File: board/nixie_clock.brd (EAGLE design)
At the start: 130 x 79 mm, 45 parts, among them Q1 BC546B, U1 AMS1117-5.0, U2 SN74141N

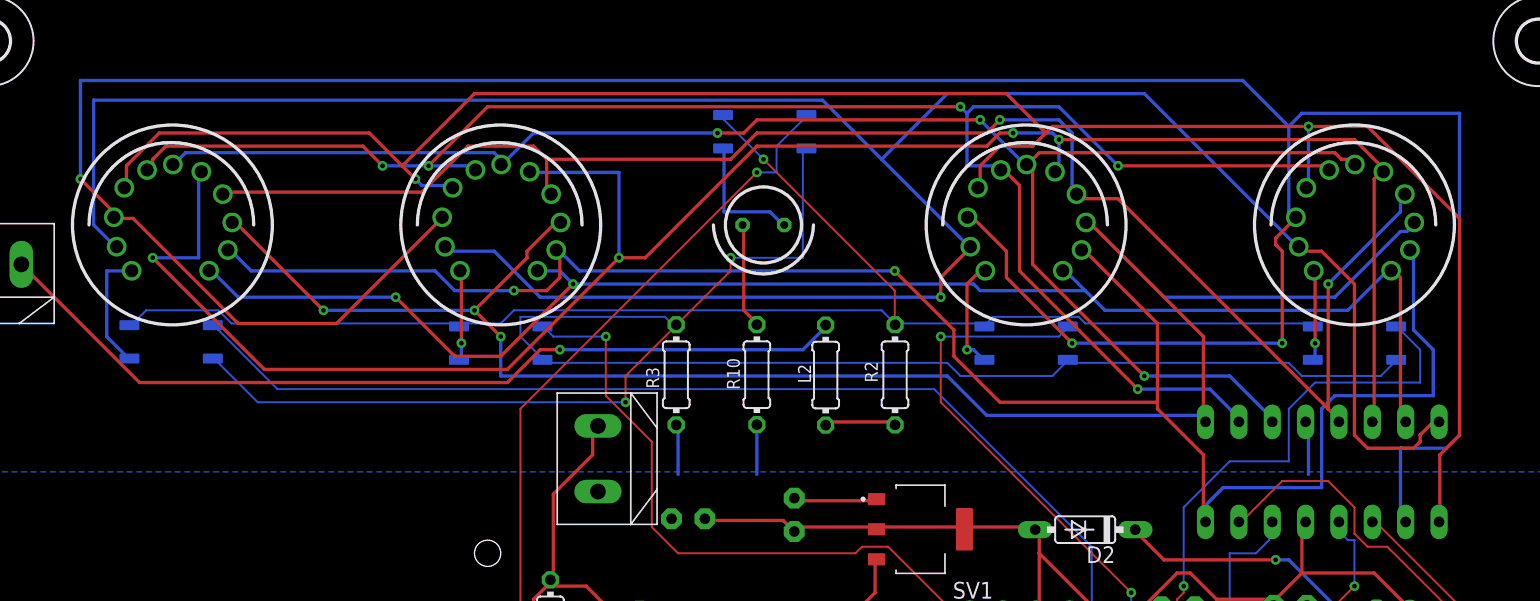
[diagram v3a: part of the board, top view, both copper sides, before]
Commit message: rounded off 90 degree wire turns
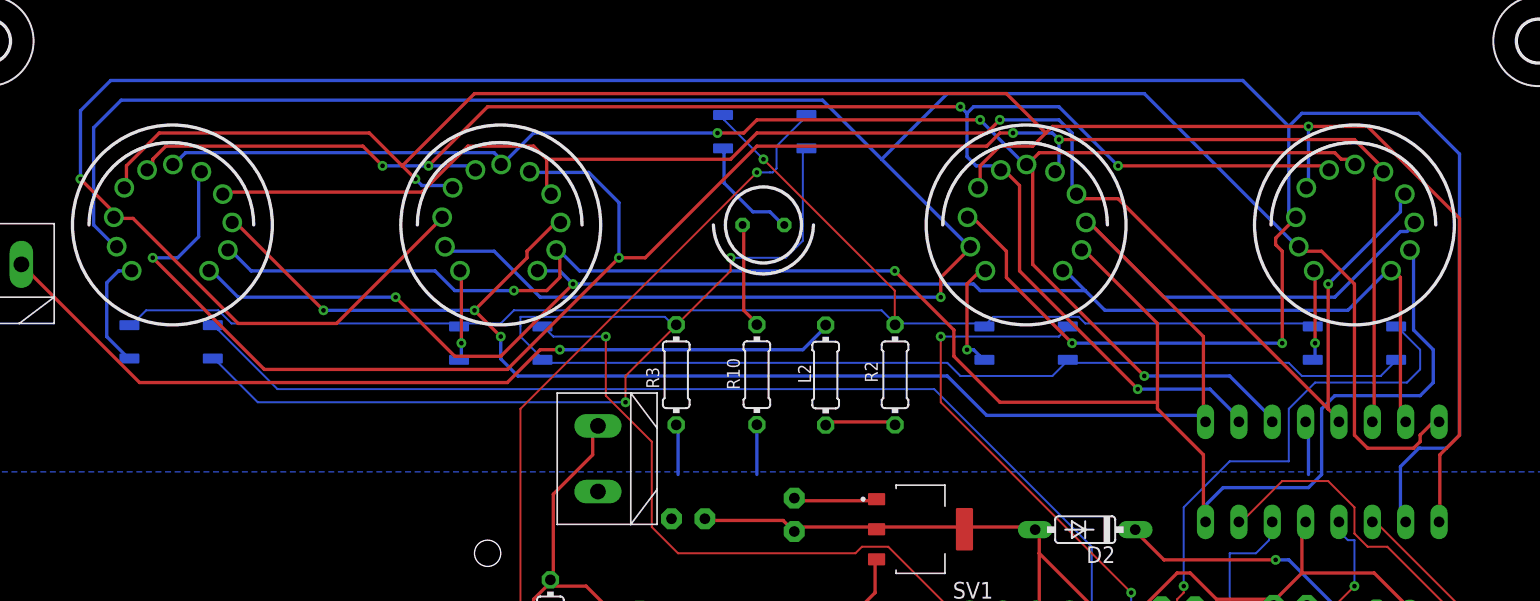
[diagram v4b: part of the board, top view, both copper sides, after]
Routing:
- net K9: track 232.2 -> 228.3 mm
- net K5: track 151.5 -> 149.2 mm
- net A_DOT: track 9.84 -> 8.55 mm
- net K0: track 191.0 -> 189.7 mm
- net K2: track 143.3 -> 142.2 mm
- net K3: track 141.0 -> 140.3 mm
- net N$16: track 144.1 -> 143.3 mm
- net N$3: track 61.8 -> 61.2 mm
- net A_10H: track 9.30 -> 8.77 mm

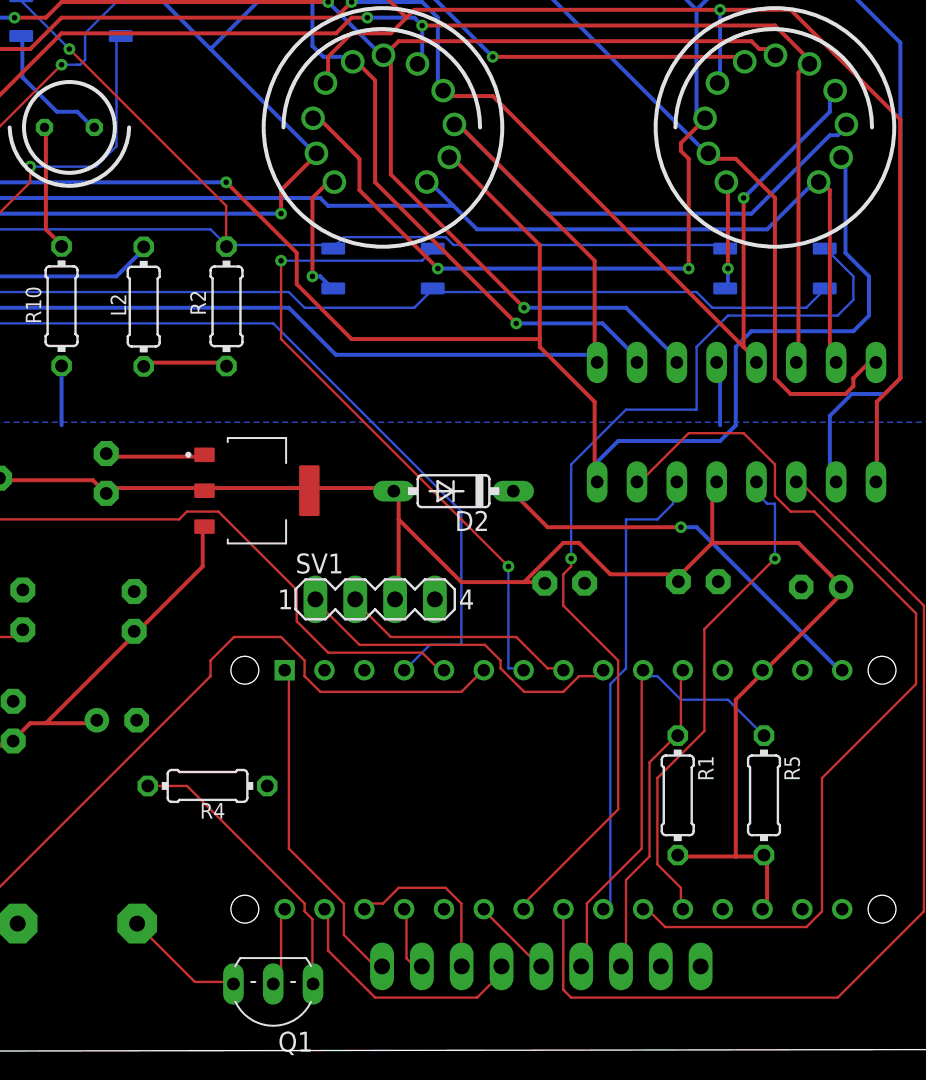
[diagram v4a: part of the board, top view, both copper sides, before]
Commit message: Connected 12V to buzzer.
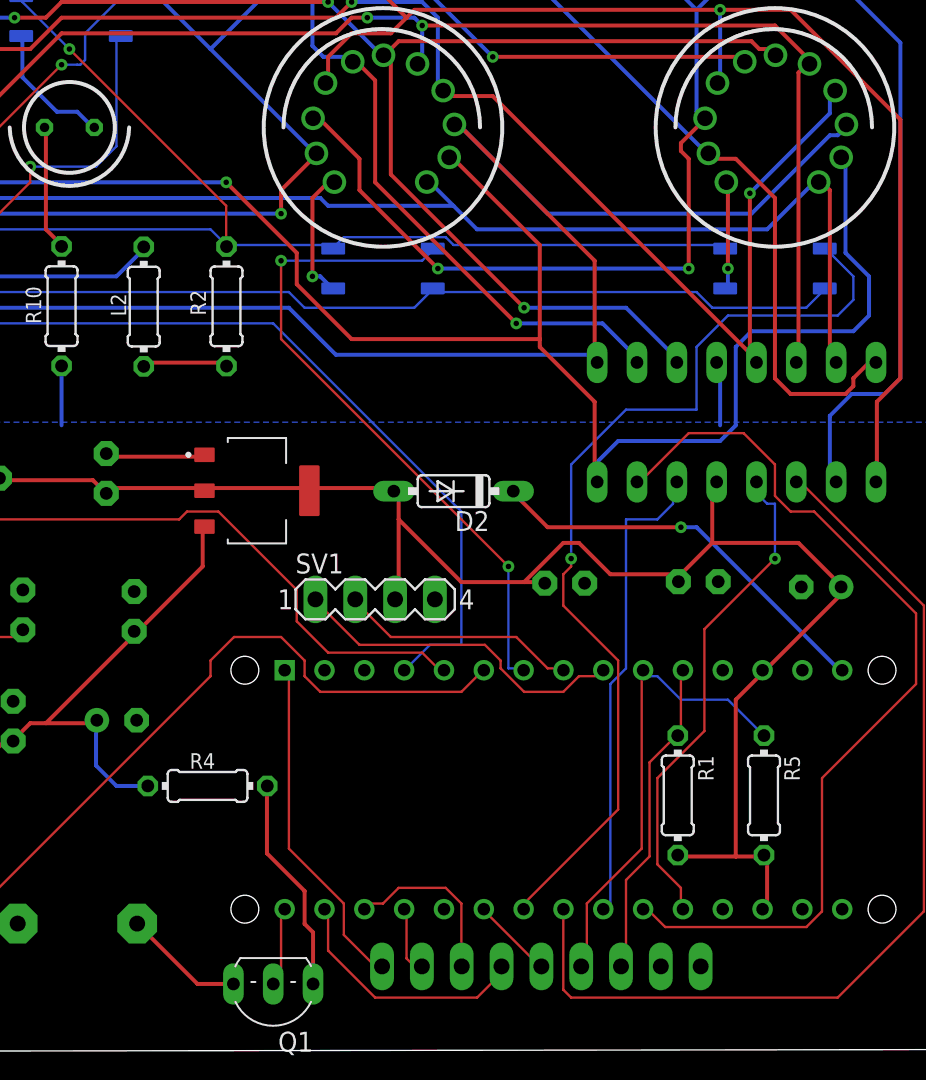
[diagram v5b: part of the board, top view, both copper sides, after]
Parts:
- turned R4 to 0 degrees
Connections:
- net +12V: now also R4.1
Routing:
- net +12V: track 42.4 -> 49.1 mm
- net N$7: track 18.4 -> 13.9 mm
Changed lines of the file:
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@@
 <attribute name="VALUE" x="58.8426" y="46.5644" size="0.9906" layer="27" ratio="10" rot="R90"/>
 </element>
-<element name="R4" library="rcl" library_urn="urn:adsk.eagle:library:334" package="0204/7" package3d_urn="urn:adsk.eagle:package:23498/2" value="100" x="73.81" y="17" smashed="yes" rot="R180">
-<attribute name="NAME" x="74.95" y="15.9046" size="0.9906" layer="25" ratio="10" rot="R180"/>
-<attribute name="POPULARITY" value="79" x="35.71" y="102.09" size="1.778" layer="27" rot="R180" display="off"/>
-<attribute name="SPICEPREFIX" value="R" x="35.71" y="102.09" size="1.778" layer="27" rot="R180" display="off"/>
-<attribute name="VALUE" x="75.4356" y="17.4826" size="0.9906" layer="27" ratio="10" rot="R180"/>
+<element name="R4" library="rcl" library_urn="urn:adsk.eagle:library:334" package="0204/7" package3d_urn="urn:adsk.eagle:package:23498/2" value="100" x="73.81" y="17" smashed="yes">
+<attribute name="NAME" x="72.67" y="18.0954" size="0.9906" layer="25" ratio="10"/>
+<attribute name="POPULARITY" value="79" x="111.91" y="-68.09" size="1.778" layer="27" display="off"/>
+<attribute name="SPICEPREFIX" value="R" x="111.91" y="-68.09" size="1.778" layer="27" display="off"/>
+<attribute name="VALUE" x="72.1844" y="16.5174" size="0.9906" layer="27" ratio="10"/>
 </element>
 <element name="U1" library="AMS1117-5.0" package="SOT229P700X180-4N" value="AMS1117-5.0" x="76.96" y="35.83" smashed="yes" rot="R270">
@@
 <wire x1="63.5" y1="21" x2="69" y2="26.5" width="0.254" layer="1"/>
 <wire x1="69" y1="26.5" x2="69.13" y2="26.86" width="0.254" layer="1"/>
+<contactref element="R4" pad="1"/>
+<wire x1="70" y1="17" x2="68" y2="17" width="0.254" layer="16"/>
+<wire x1="68" y1="17" x2="66.7" y2="18.3" width="0.254" layer="16"/>
+<wire x1="66.7" y1="18.3" x2="66.7" y2="21.14" width="0.254" layer="16"/>
+<wire x1="66.7" y1="21.14" x2="66.75" y2="21.19" width="0.254" layer="16"/>
 </signal>
 <signal name="+5V" class="1">
@@
 <wire x1="24" y1="61.5" x2="23.8374" y2="61.3476" width="0.254" layer="1"/>
 <wire x1="48.5" y1="61.5" x2="48.8374" y2="61.3476" width="0.254" layer="1"/>
-<wire x1="92" y1="61" x2="108" y2="45" width="0.254" layer="1"/>
-<wire x1="108" y1="45" x2="108.5" y2="44.5" width="0.254" layer="1"/>
+<wire x1="92" y1="61" x2="108.4" y2="44.6" width="0.254" layer="1"/>
+<wire x1="108.4" y1="44.6" x2="108.5" y2="44.5" width="0.254" layer="1"/>
 <wire x1="89" y1="61" x2="92" y2="61" width="0.254" layer="1"/>
 <wire x1="108.5" y1="44.5" x2="108.82" y2="44.01" width="0.254" layer="1"/>
 <wire x1="89" y1="61" x2="88.8374" y2="61.3476" width="0.254" layer="1"/>
-<wire x1="113.5" y1="60" x2="113.5" y2="61" width="0.254" layer="16"/>
-<wire x1="108" y1="54.5" x2="113.5" y2="60" width="0.254" layer="16"/>
-<wire x1="108" y1="45" x2="108" y2="54.5" width="0.254" layer="1"/>
+<wire x1="113.5" y1="59.9" x2="113.5" y2="61" width="0.254" layer="16"/>
+<wire x1="108.4" y1="54.8" x2="113.5" y2="59.9" width="0.254" layer="16"/>
+<wire x1="108.4" y1="44.6" x2="108.4" y2="54.8" width="0.254" layer="1"/>
 <wire x1="113.5" y1="61" x2="113.8374" y2="61.3476" width="0.254" layer="16"/>
 <wire x1="62.5" y1="64" x2="48.5" y2="64" width="0.254" layer="1"/>
@@
 <wire x1="88.5" y1="61.5" x2="88.5" y2="66" width="0.254" layer="16"/>
 <wire x1="88.5" y1="61.5" x2="88.8374" y2="61.3476" width="0.254" layer="16"/>
-<via x="108" y="54.5" extent="1-16" drill="0.35"/>
+<via x="108.4" y="54.8" extent="1-16" drill="0.35"/>
 <via x="83" y="67" extent="1-16" drill="0.35"/>
 </signal>
@@
 <contactref element="R4" pad="2"/>
 <contactref element="Q1" pad="C"/>
-<wire x1="80.5" y1="8.5" x2="80.5" y2="4.5" width="0.1524" layer="1"/>
-<wire x1="80" y1="9" x2="80.5" y2="8.5" width="0.1524" layer="1"/>
-<wire x1="80" y1="9.5" x2="80" y2="9" width="0.1524" layer="1"/>
-<wire x1="72.5" y1="17" x2="80" y2="9.5" width="0.1524" layer="1"/>
-<wire x1="70" y1="17" x2="72.5" y2="17" width="0.1524" layer="1"/>
-<wire x1="80.5" y1="4.5" x2="80.54" y2="4.37" width="0.1524" layer="1"/>
+<wire x1="80.54" y1="4.37" x2="80.54" y2="7.66" width="0.254" layer="1"/>
+<wire x1="80" y1="8.2" x2="80" y2="10.3" width="0.254" layer="1"/>
+<wire x1="80" y1="10.3" x2="77.6" y2="12.7" width="0.254" layer="1"/>
+<wire x1="80.54" y1="7.66" x2="80" y2="8.2" width="0.254" layer="1"/>
+<wire x1="77.6" y1="16.98" x2="77.62" y2="17" width="0.254" layer="1"/>
+<wire x1="77.6" y1="12.7" x2="77.6" y2="16.98" width="0.254" layer="1"/>
 </signal>
 <signal name="BUZ_IN">
 <contactref element="Q1" pad="E"/>
 <contactref element="BUZZER" pad="+"/>
-<wire x1="73" y1="4.5" x2="75" y2="4.5" width="0.1524" layer="1"/>
-<wire x1="69.5" y1="8" x2="73" y2="4.5" width="0.1524" layer="1"/>
-<wire x1="75" y1="4.5" x2="75.46" y2="4.37" width="0.1524" layer="1"/>
-<wire x1="69.5" y1="8" x2="69.32" y2="8.22" width="0.1524" layer="1"/>
+<wire x1="69.32" y1="8.22" x2="73.17" y2="4.37" width="0.254" layer="1"/>
+<wire x1="73.17" y1="4.37" x2="75.46" y2="4.37" width="0.254" layer="1"/>
 </signal>
 <signal name="BUZ_SGN">

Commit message: added nixie tube testing script.
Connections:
- net N$11 renamed D
- net N$12 renamed C
- net N$13 renamed B
- net N$14 renamed A
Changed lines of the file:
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@@
 <wire x1="46.5" y1="51.5" x2="46.5" y2="51.5" width="0.1524" layer="16"/>
 </signal>
-<signal name="N$11">
+<signal name="D">
 <contactref element="U2" pad="4"/>
 <contactref element="ARDUINO_NANO" pad="20"/>
@@
 <via x="110" y="31.5" extent="1-16" drill="0.35"/>
 </signal>
-<signal name="N$12">
+<signal name="C">
 <contactref element="U2" pad="7"/>
 <contactref element="ARDUINO_NANO" pad="21"/>
@@
 <wire x1="101.5" y1="36.5" x2="101.2" y2="36.39" width="0.1524" layer="1"/>
 </signal>
-<signal name="N$13">
+<signal name="B">
 <contactref element="U2" pad="6"/>
 <contactref element="ARDUINO_NANO" pad="22"/>
@@
 <wire x1="103.5" y1="36" x2="103.74" y2="36.39" width="0.1524" layer="16"/>
 </signal>
-<signal name="N$14">
+<signal name="A">
 <contactref element="U2" pad="3"/>
 <contactref element="ARDUINO_NANO" pad="23"/>
